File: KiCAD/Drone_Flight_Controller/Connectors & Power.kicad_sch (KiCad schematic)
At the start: 58 parts, among them J1 Conn_01x05, J301 Conn_01x03_Pin, J302 Conn_01x04, J303 Conn_01x03_Pin, J304 XT60, J305 Conn_01x03_Pin, J306 Conn_01x03_Pin, Q301 BC846C, Q302 BC846C, Q303 BC856C, Q304 BC846C, Q305 BC856C, Q306 BC856C, Q307 BC856C, Q309 BC846C, U202 AS358, U203 AS358, U301 AS358, U302 AS358, U305 AS358

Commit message: Reannotate
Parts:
- renumbered C301 to C201, C302 to C202, C303 to C203, C304 to C204, C305 to C205, C306 to C206, C307 to C207, C308 to C208, C309 to C209, C310 to C210, D4 to D201, D7 to D202, D8 to D203, D3 to D204, D13 to D205, D14 to D206, D2 to D207, D9 to D208, D10 to D209, D1 to D210, D11 to D211, D12 to D212, D18 to D213, D15 to D214, D16 to D215, H301 to H201, H302 to H202, H303 to H203, H304 to H204, J302 to J201, J301 to J202, J303 to J203, J305 to J204, J304 to J205, J306 to J206, J1 to J207, Q309 to Q201, Q303 to Q202, Q301 to Q203, Q305 to Q204, Q302 to Q205, Q306 to Q206, Q304 to Q207, Q307 to Q208, R3 to R201, R301 to R202, R302 to R203, R4 to R204, R5 to R205, R6 to R206, R7 to R207, R8 to R208, R9 to R209, U301 to U201, U305 to U202, U202 to U203, U203 to U204, U302 to U205

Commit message: Copy footprints to new parts
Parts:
- R201, R204, R205, R206: footprint (none) -> Resistor_SMD:R_0805_2012Metric_Pad1.20x1.40mm_HandSolder; Link (none) -> https://www.mouser.at/ProductDetail/KOA-Speer/RN73R2ATTD100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
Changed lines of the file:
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@@
 			)
 		)
-		(property "Footprint" ""
+		(property "Footprint" "Resistor_SMD:R_0805_2012Metric_Pad1.20x1.40mm_HandSolder"
 			(at 187.96 74.168 90)
 			(effects
@@
 			)
 		)
-		(property "Datasheet" "~"
+		(property "Datasheet" "https://www.mouser.com/catalog/specsheets/KOA_Speer_RN73R__8_20_24.pdf"
 			(at 187.96 72.39 0)
 			(effects
@@
 			)
 		)
+		(property "Link" "https://www.mouser.at/ProductDetail/KOA-Speer/RN73R2ATTD1002B25?qs=sGAEpiMZZMtlubZbdhIBIMWCRdMSCzTZYWNHqlmKHZA%3D"
+			(at 187.96 72.39 90)
+			(effects
+				(font
+					(size 1.27 1.27)
+				)
+				(hide yes)
+			)
+		)
 		(pin "1"
 		)
@@
 			)
 		)
-		(property "Footprint" ""
+		(property "Footprint" "Resistor_SMD:R_0805_2012Metric_Pad1.20x1.40mm_HandSolder"
 			(at 187.96 140.208 90)
 			(effects
@@
 			)
 		)
-		(property "Datasheet" "~"
+		(property "Datasheet" "https://www.mouser.com/catalog/specsheets/KOA_Speer_RN73R__8_20_24.pdf"
 			(at 187.96 138.43 0)
 			(effects
@@
 			)
 		)
+		(property "Link" "https://www.mouser.at/ProductDetail/KOA-Speer/RN73R2ATTD1002B25?qs=sGAEpiMZZMtlubZbdhIBIMWCRdMSCzTZYWNHqlmKHZA%3D"
+			(at 187.96 138.43 90)
+			(effects
+				(font
+					(size 1.27 1.27)
+				)
+				(hide yes)
+			)
+		)
 		(pin "1"
 		)
@@
 			)
 		)
-		(property "Footprint" ""
+		(property "Footprint" "Resistor_SMD:R_0805_2012Metric_Pad1.20x1.40mm_HandSolder"
 			(at 187.96 41.148 90)
 			(effects
@@
 			)
 		)
-		(property "Datasheet" "~"
+		(property "Datasheet" "https://www.mouser.com/catalog/specsheets/KOA_Speer_RN73R__8_20_24.pdf"
 			(at 187.96 39.37 0)
 			(effects
@@
 			)
 		)
+		(property "Link" "https://www.mouser.at/ProductDetail/KOA-Speer/RN73R2ATTD1002B25?qs=sGAEpiMZZMtlubZbdhIBIMWCRdMSCzTZYWNHqlmKHZA%3D"
+			(at 187.96 39.37 90)
+			(effects
+				(font
+					(size 1.27 1.27)
+				)
+				(hide yes)
+			)
+		)
 		(pin "1"
 		)
@@
 			)
 		)
-		(property "Footprint" ""
+		(property "Footprint" "Resistor_SMD:R_0805_2012Metric_Pad1.20x1.40mm_HandSolder"
 			(at 187.96 107.188 90)
 			(effects
@@
 			)
 		)
-		(property "Datasheet" "~"
+		(property "Datasheet" "https://www.mouser.com/catalog/specsheets/KOA_Speer_RN73R__8_20_24.pdf"
 			(at 187.96 105.41 0)
 			(effects
@@
 			(effects
 				(font
+					(size 1.27 1.27)
+				)
+				(hide yes)
+			)
+		)
+		(property "Link" "https://www.mouser.at/ProductDetail/KOA-Speer/RN73R2ATTD1002B25?qs=sGAEpiMZZMtlubZbdhIBIMWCRdMSCzTZYWNHqlmKHZA%3D"
+			(at 187.96 105.41 90)
+			(effects
+				(font

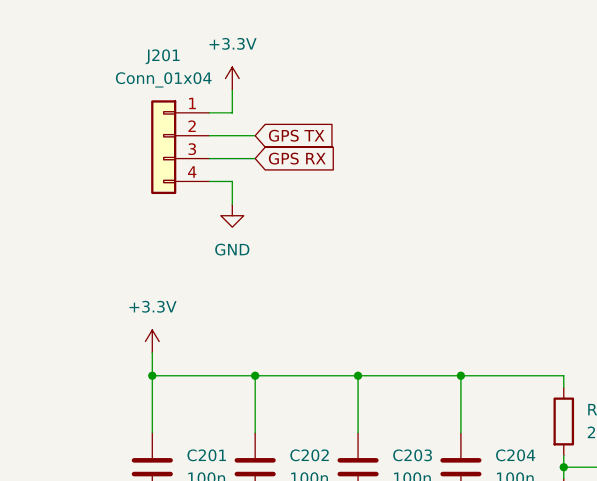
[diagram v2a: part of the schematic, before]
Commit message: Change "+3.3V" to "+3V3" for consistency
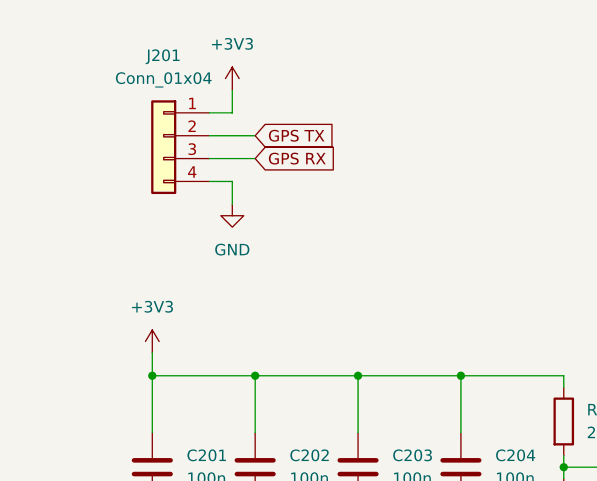
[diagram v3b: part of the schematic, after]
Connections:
- net +3.3V is gone; now on net +3V3: C201.1, C202.1, C203.1, C204.1, J201.1 (Pin_1), R202.1
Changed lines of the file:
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@@
 			)
 		)
-		(property "Value" "+3.3V"
+		(property "Value" "+3V3"
 			(at 31.75 46.99 0)
 			(effects
@@
 			)
 		)
-		(property "Value" "+3.3V"
+		(property "Value" "+3V3"
 			(at 40.64 17.78 0)
 			(effects

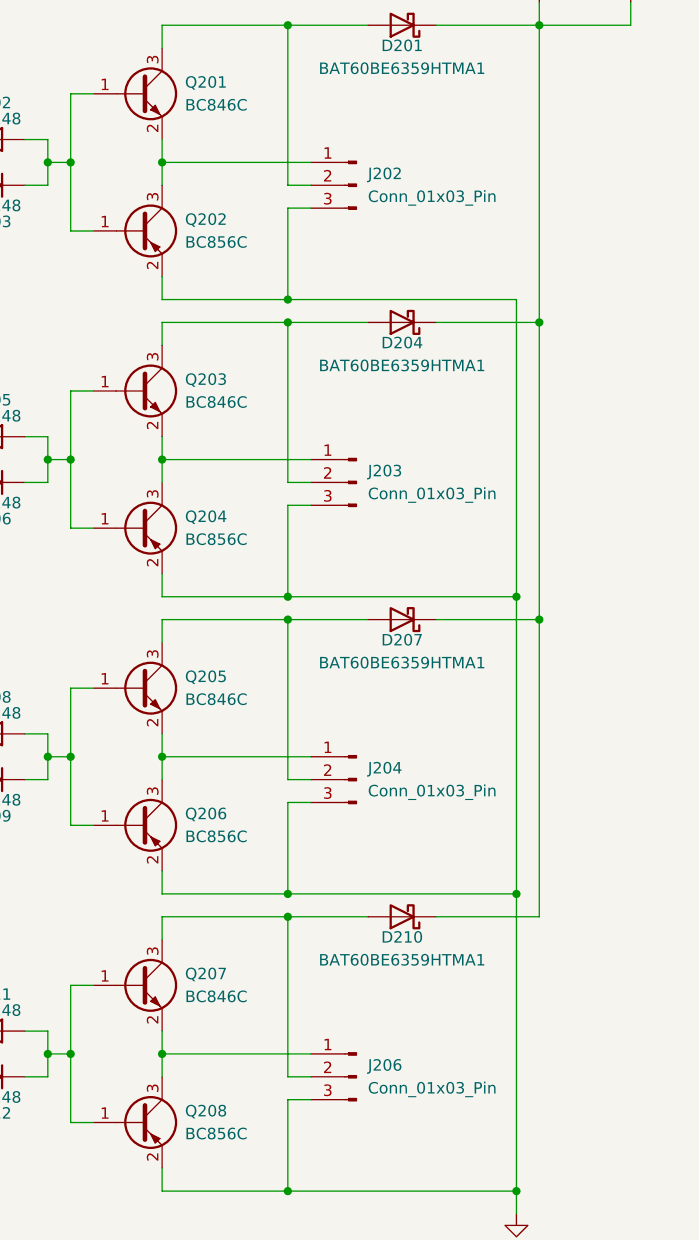
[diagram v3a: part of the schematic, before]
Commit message: Rename connectors to Motor[1..4]
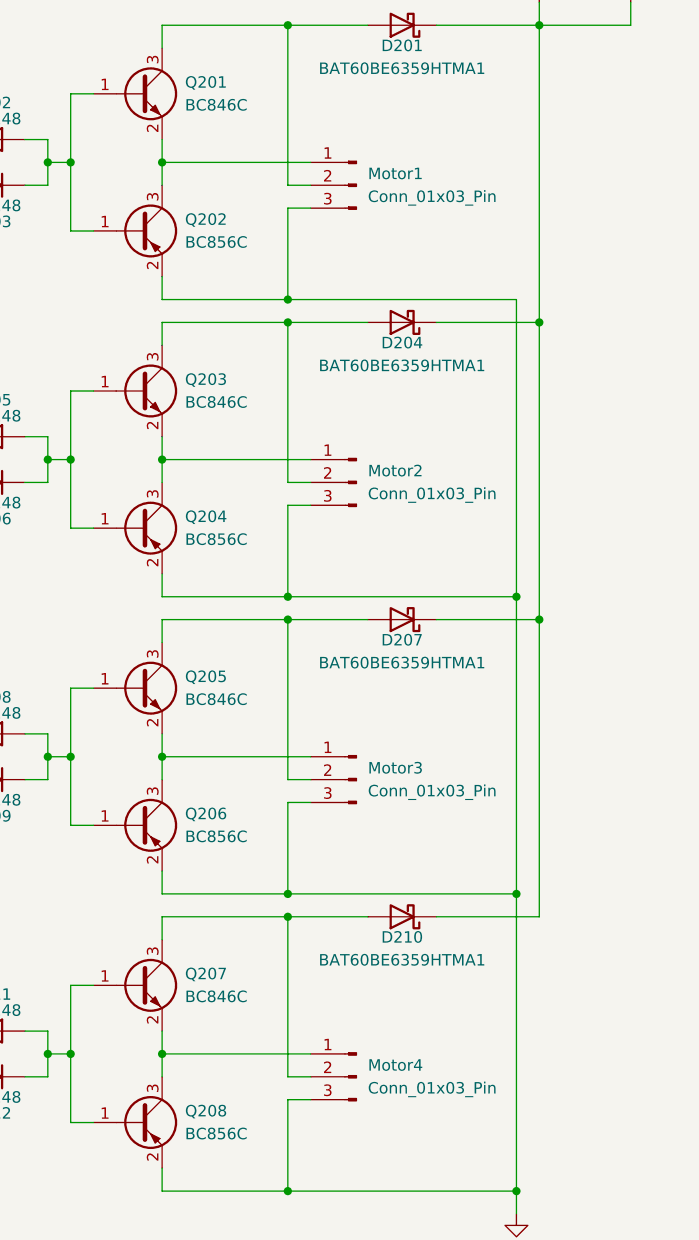
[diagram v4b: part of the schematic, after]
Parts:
- renumbered J202 to Motor1, J203 to Motor2, J204 to Motor3, J206 to Motor4
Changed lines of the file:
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@@
 		(dnp no)
 		(fields_autoplaced yes)
-		(property "Reference" "J206"
+		(property "Reference" "Motor4"
 			(at 242.57 139.6999 0)
 			(effects
@@
 			(project "Drone_Flight_Controller"
 				(path "/05daaa24-e506-4b9a-9564-8bf799413ca8/260564b2-f35d-47a6-9418-8c7c5bce9239"
-					(reference "J206")
+					(reference "Motor4")
 					(unit 1)
 				)
@@
 		(dnp no)
 		(fields_autoplaced yes)
-		(property "Reference" "J203"
+		(property "Reference" "Motor2"
 			(at 242.57 73.6599 0)
 			(effects
@@
 			(project "Drone_Flight_Controller"
 				(path "/05daaa24-e506-4b9a-9564-8bf799413ca8/260564b2-f35d-47a6-9418-8c7c5bce9239"
-					(reference "J203")
+					(reference "Motor2")
 					(unit 1)
 				)
@@
 		(dnp no)
 		(fields_autoplaced yes)
-		(property "Reference" "J202"
+		(property "Reference" "Motor1"
 			(at 242.57 40.6399 0)
 			(effects
@@
 			(project ""
 				(path "/05daaa24-e506-4b9a-9564-8bf799413ca8/260564b2-f35d-47a6-9418-8c7c5bce9239"
-					(reference "J202")
+					(reference "Motor1")
 					(unit 1)
 				)
@@
 		(dnp no)
 		(fields_autoplaced yes)
-		(property "Reference" "J204"
+		(property "Reference" "Motor3"
 			(at 242.57 106.6799 0)
 			(effects
@@
 			(project "Drone_Flight_Controller"
 				(path "/05daaa24-e506-4b9a-9564-8bf799413ca8/260564b2-f35d-47a6-9418-8c7c5bce9239"
-					(reference "J204")
+					(reference "Motor3")
 					(unit 1)
 				)

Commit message: Change footprints to HandSoldering
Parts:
- D201, D204, D207, D210: footprint Diode_SMD:D_SOD-323F -> Diode_SMD:D_SOD-323_HandSoldering
- D202, D203, D205, D206, D208, D209, D211, D212: footprint Diode_THT:D_DO-35_SOD27_P7.62mm_Horizontal -> Diode_SMD:D_SOD-323_HandSoldering; Link https://www.mouser.at/ProductDetail/onsemi-Fairchild/1N4148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 -> https://www.mouser.at/ProductDetail/Taiwan-Semiconductor/1N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
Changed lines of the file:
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@@
 			)
 		)
-		(property "Footprint" "Diode_SMD:D_SOD-323F"
+		(property "Footprint" "Diode_SMD:D_SOD-323_HandSoldering"
 			(at 246.38 123.19 0)
 			(effects
@@
 			)
 		)
-		(property "Footprint" "Diode_THT:D_DO-35_SOD27_P7.62mm_Horizontal"
+		(property "Footprint" "Diode_SMD:D_SOD-323_HandSoldering"
 			(at 200.66 102.87 0)
 			(effects
@@
 			)
 		)
-		(property "Datasheet" "https://www.mouser.at/datasheet/2/308/1/1N914_D-3574539.pdf"
+		(property "Datasheet" "https://www.taiwansemi.com/assets/datasheet/pdf.php?pn=1N4148WS"
 			(at 200.66 102.87 0)
 			(effects
@@
 			)
 		)
-		(property "Link" "https://www.mouser.at/ProductDetail/onsemi-Fairchild/1N4148?qs=i4Fj9T%2FoRm8RMUhj5DeFQg%3D%3D"
+		(property "Link" "https://www.mouser.at/ProductDetail/Taiwan-Semiconductor/1N4148WS-RRG?qs=KwaGCOX4wIbeBaq5Ynva5w%3D%3D"
 			(at 200.66 102.87 0)
 			(effects
@@
 			)
 		)
-		(property "Footprint" "Diode_SMD:D_SOD-323F"
+		(property "Footprint" "Diode_SMD:D_SOD-323_HandSoldering"
 			(at 246.38 90.17 0)
 			(effects
@@
 			)
 		)
-		(property "Footprint" "Diode_THT:D_DO-35_SOD27_P7.62mm_Horizontal"
+		(property "Footprint" "Diode_SMD:D_SOD-323_HandSoldering"
 			(at 200.66 107.95 0)
 			(effects
@@
 			)
 		)
-		(property "Datasheet" "https://www.mouser.at/datasheet/2/308/1/1N914_D-3574539.pdf"
+		(property "Datasheet" "https://www.taiwansemi.com/assets/datasheet/pdf.php?pn=1N4148WS"
 			(at 200.66 107.95 0)
 			(effects
@@
 			)
 		)
-		(property "Link" "https://www.mouser.at/ProductDetail/onsemi-Fairchild/1N4148?qs=i4Fj9T%2FoRm8RMUhj5DeFQg%3D%3D"
+		(property "Link" "https://www.mouser.at/ProductDetail/Taiwan-Semiconductor/1N4148WS-RRG?qs=KwaGCOX4wIbeBaq5Ynva5w%3D%3D"
 			(at 200.66 107.95 0)
 			(effects
@@
 			)
 		)
-		(property "Footprint" "Diode_THT:D_DO-35_SOD27_P7.62mm_Horizontal"
+		(property "Footprint" "Diode_SMD:D_SOD-323_HandSoldering"
 			(at 200.66 140.97 0)
 			(effects
@@
 			)
 		)
-		(property "Datasheet" "https://www.mouser.at/datasheet/2/308/1/1N914_D-3574539.pdf"
+		(property "Datasheet" "https://www.taiwansemi.com/assets/datasheet/pdf.php?pn=1N4148WS"
 			(at 200.66 140.97 0)
 			(effects
@@
 			)
 		)
-		(property "Link" "https://www.mouser.at/ProductDetail/onsemi-Fairchild/1N4148?qs=i4Fj9T%2FoRm8RMUhj5DeFQg%3D%3D"
+		(property "Link" "https://www.mouser.at/ProductDetail/Taiwan-Semiconductor/1N4148WS-RRG?qs=KwaGCOX4wIbeBaq5Ynva5w%3D%3D"
 			(at 200.66 140.97 0)
 			(effects
@@
 			)
 		)
-		(property "Footprint" "Diode_SMD:D_SOD-323F"
+		(property "Footprint" "Diode_SMD:D_SOD-323_HandSoldering"
 			(at 246.38 24.13 0)
 			(effects
@@
 			)
 		)
-		(property "Footprint" "Diode_THT:D_DO-35_SOD27_P7.62mm_Horizontal"
+		(property "Footprint" "Diode_SMD:D_SOD-323_HandSoldering"
 			(at 200.66 135.89 0)
 			(effects
@@
 			)
 		)
-		(property "Datasheet" "https://www.mouser.at/datasheet/2/308/1/1N914_D-3574539.pdf"
+		(property "Datasheet" "https://www.taiwansemi.com/assets/datasheet/pdf.php?pn=1N4148WS"
 			(at 200.66 135.89 0)
 			(effects
@@
 			)
 		)
-		(property "Link" "https://www.mouser.at/ProductDetail/onsemi-Fairchild/1N4148?qs=i4Fj9T%2FoRm8RMUhj5DeFQg%3D%3D"
+		(property "Link" "https://www.mouser.at/ProductDetail/Taiwan-Semiconductor/1N4148WS-RRG?qs=KwaGCOX4wIbeBaq5Ynva5w%3D%3D"
 			(at 200.66 135.89 0)
 			(effects
@@
 			)
 		)
-		(property "Footprint" "Diode_THT:D_DO-35_SOD27_P7.62mm_Horizontal"
+		(property "Footprint" "Diode_SMD:D_SOD-323_HandSoldering"
 			(at 200.66 69.85 0)
 			(effects
@@
 			)
 		)
-		(property "Datasheet" "https://www.mouser.at/datasheet/2/308/1/1N914_D-3574539.pdf"
+		(property "Datasheet" "https://www.taiwansemi.com/assets/datasheet/pdf.php?pn=1N4148WS"
 			(at 200.66 69.85 0)
 			(effects
@@
 			)
 		)
-		(property "Link" "https://www.mouser.at/ProductDetail/onsemi-Fairchild/1N4148?qs=i4Fj9T%2FoRm8RMUhj5DeFQg%3D%3D"
+		(property "Link" "https://www.mouser.at/ProductDetail/Taiwan-Semiconductor/1N4148WS-RRG?qs=KwaGCOX4wIbeBaq5Ynva5w%3D%3D"
 			(at 200.66 69.85 0)
 			(effects
@@
 			)
 		)
-		(property "Footprint" "Diode_SMD:D_SOD-323F"
+		(property "Footprint" "Diode_SMD:D_SOD-323_HandSoldering"
 			(at 246.38 57.15 0)
 			(effects
@@
 			)
 		)
-		(property "Footprint" "Diode_THT:D_DO-35_SOD27_P7.62mm_Horizontal"
+		(property "Footprint" "Diode_SMD:D_SOD-323_HandSoldering"
 			(at 200.66 36.83 0)
 			(effects
@@
 			)
 		)
-		(property "Datasheet" "https://www.mouser.at/datasheet/2/308/1/1N914_D-3574539.pdf"
+		(property "Datasheet" "https://www.taiwansemi.com/assets/datasheet/pdf.php?pn=1N4148WS"
 			(at 200.66 36.83 0)
 			(effects
@@
 			)
 		)
-		(property "Link" "https://www.mouser.at/ProductDetail/onsemi-Fairchild/1N4148?qs=i4Fj9T%2FoRm8RMUhj5DeFQg%3D%3D"
+		(property "Link" "https://www.mouser.at/ProductDetail/Taiwan-Semiconductor/1N4148WS-RRG?qs=KwaGCOX4wIbeBaq5Ynva5w%3D%3D"
 			(at 200.66 36.83 0)
 			(effects
@@
 			)
 		)
-		(property "Footprint" "Diode_THT:D_DO-35_SOD27_P7.62mm_Horizontal"
+		(property "Footprint" "Diode_SMD:D_SOD-323_HandSoldering"
 			(at 200.66 74.93 0)
 			(effects
@@
 			)
 		)
-		(property "Datasheet" "https://www.mouser.at/datasheet/2/308/1/1N914_D-3574539.pdf"
+		(property "Datasheet" "https://www.taiwansemi.com/assets/datasheet/pdf.php?pn=1N4148WS"
 			(at 200.66 74.93 0)
 			(effects
@@
 			)
 		)
-		(property "Link" "https://www.mouser.at/ProductDetail/onsemi-Fairchild/1N4148?qs=i4Fj9T%2FoRm8RMUhj5DeFQg%3D%3D"
+		(property "Link" "https://www.mouser.at/ProductDetail/Taiwan-Semiconductor/1N4148WS-RRG?qs=KwaGCOX4wIbeBaq5Ynva5w%3D%3D"
 			(at 200.66 74.93 0)
 			(effects
@@
 			)
 		)
-		(property "Footprint" "Diode_THT:D_DO-35_SOD27_P7.62mm_Horizontal"
+		(property "Footprint" "Diode_SMD:D_SOD-323_HandSoldering"
 			(at 200.66 41.91 0)
 			(effects
@@
 			)
 		)
-		(property "Datasheet" "https://www.mouser.at/datasheet/2/308/1/1N914_D-3574539.pdf"
+		(property "Datasheet" "https://www.taiwansemi.com/assets/datasheet/pdf.php?pn=1N4148WS"
 			(at 200.66 41.91 0)
 			(effects
@@
 			)
 		)
-		(property "Link" "https://www.mouser.at/ProductDetail/onsemi-Fairchild/1N4148?qs=i4Fj9T%2FoRm8RMUhj5DeFQg%3D%3D"
+		(property "Link" "https://www.mouser.at/ProductDetail/Taiwan-Semiconductor/1N4148WS-RRG?qs=KwaGCOX4wIbeBaq5Ynva5w%3D%3D"
 			(at 200.66 41.91 0)
 			(effects

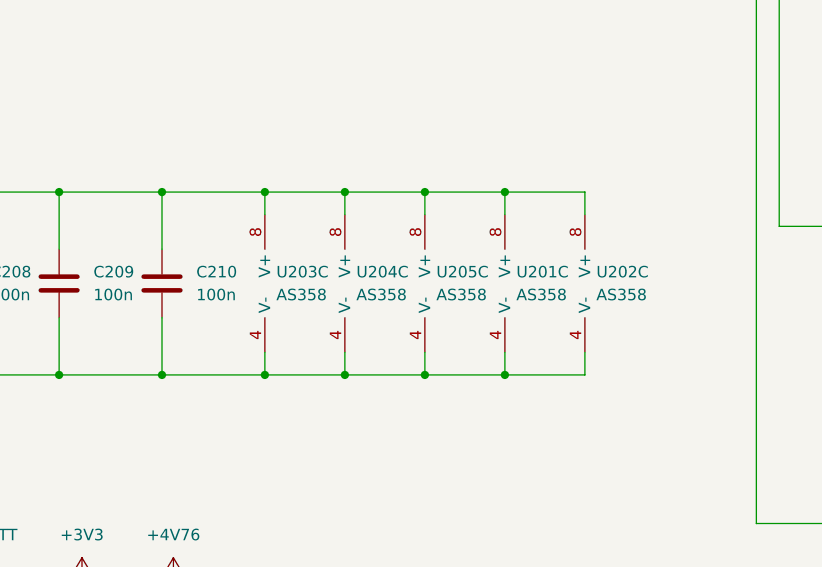
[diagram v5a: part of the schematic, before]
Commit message: Remove unneaded OPAMPs
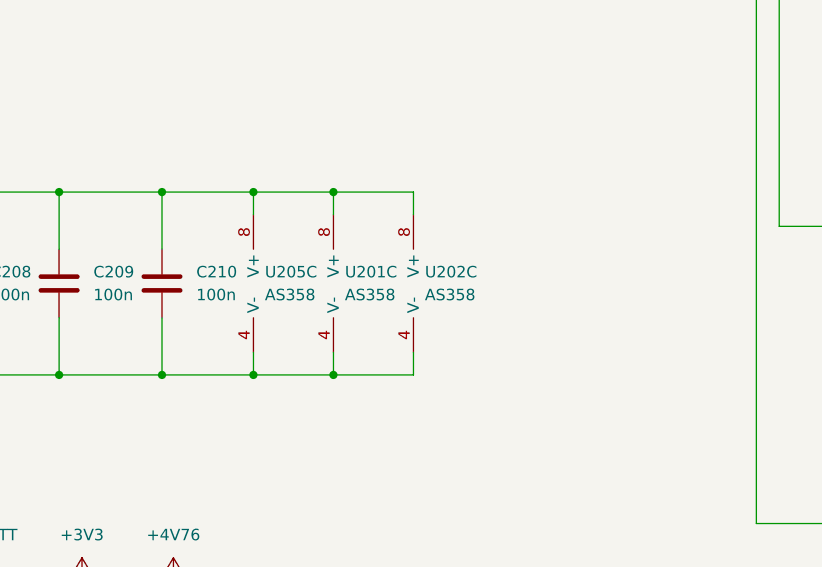
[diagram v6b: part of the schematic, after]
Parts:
- removed U203, U204: AS358, Package_SO:SO-8_3.9x4.9mm_P1.27mm, symbol Device:Opamp_Dual
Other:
- moved on the sheet: U201C, U202C, U205C

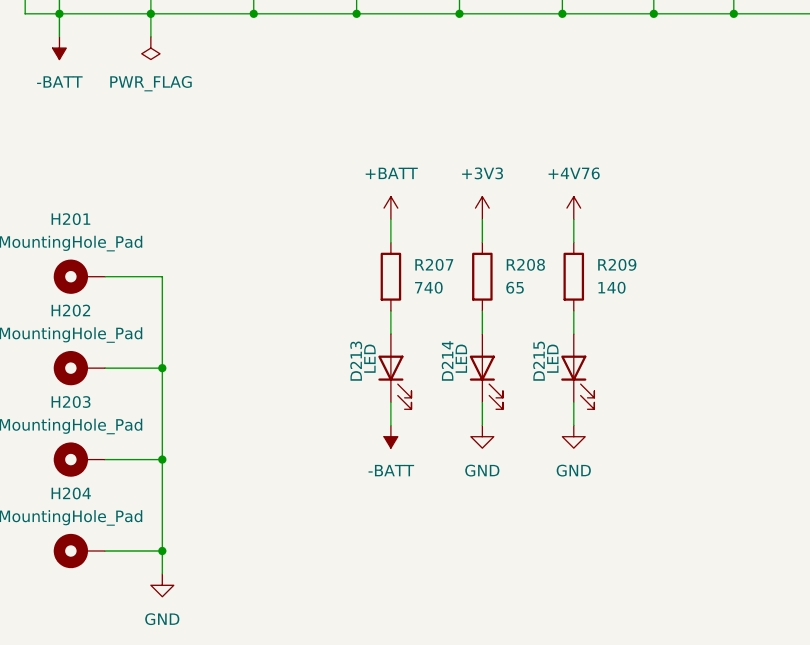
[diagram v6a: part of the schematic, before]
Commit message: Remove battery LED for power draw reasons
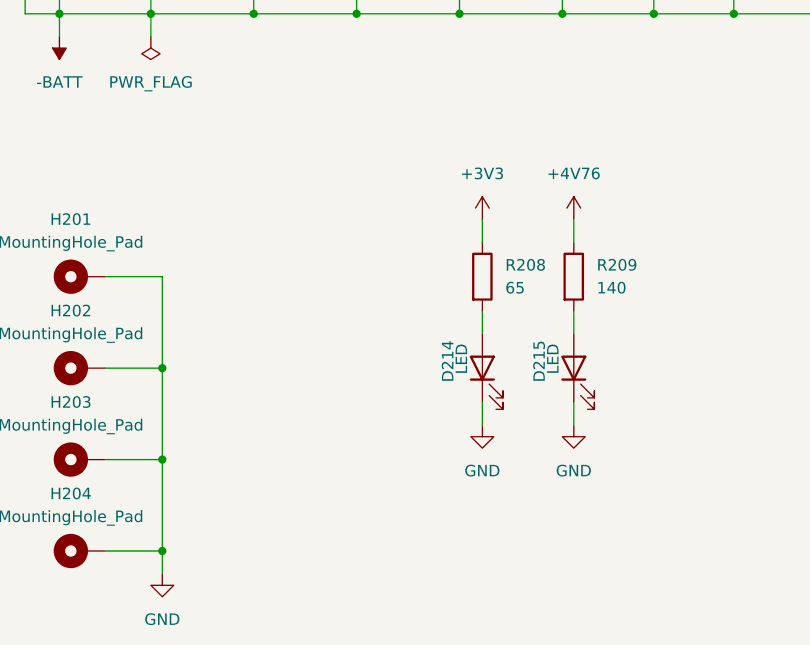
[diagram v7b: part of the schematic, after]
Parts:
- removed D213: LED, LED_SMD:LED_0805_2012Metric_Pad1.15x1.40mm_HandSolder, symbol Device:LED
- removed R207: 740, symbol Device:R
- J207: footprint (none) -> Connector_PinHeader_2.54mm:PinHeader_1x05_P2.54mm_Vertical
